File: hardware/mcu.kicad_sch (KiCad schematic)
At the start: 32 parts, among them J3 SW, SW1 BTN_ACT, SW2 BTN_DEACT, U1 STM32F103C8T6, Y1 32KHz, Y2 8MHz

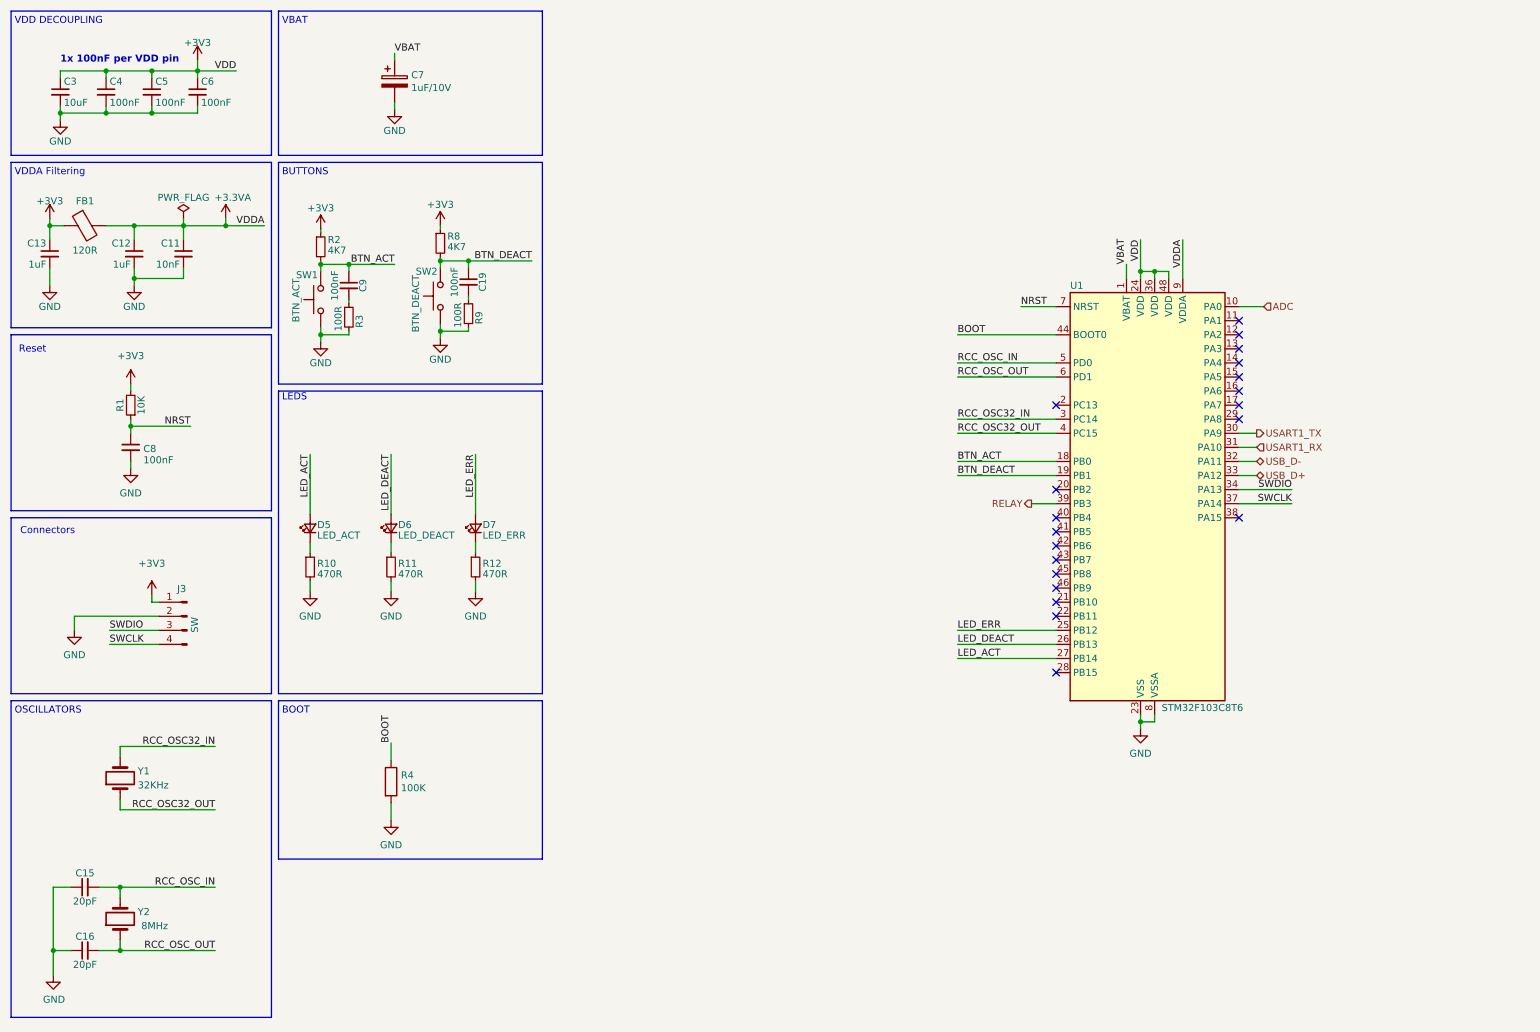
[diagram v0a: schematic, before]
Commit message: * Added an EXP port (contains SPI/I2C/UART/2PINS GPIO/3V3/5V) to the MCU module * USB port connections completed * The Modules are connected to MCU module
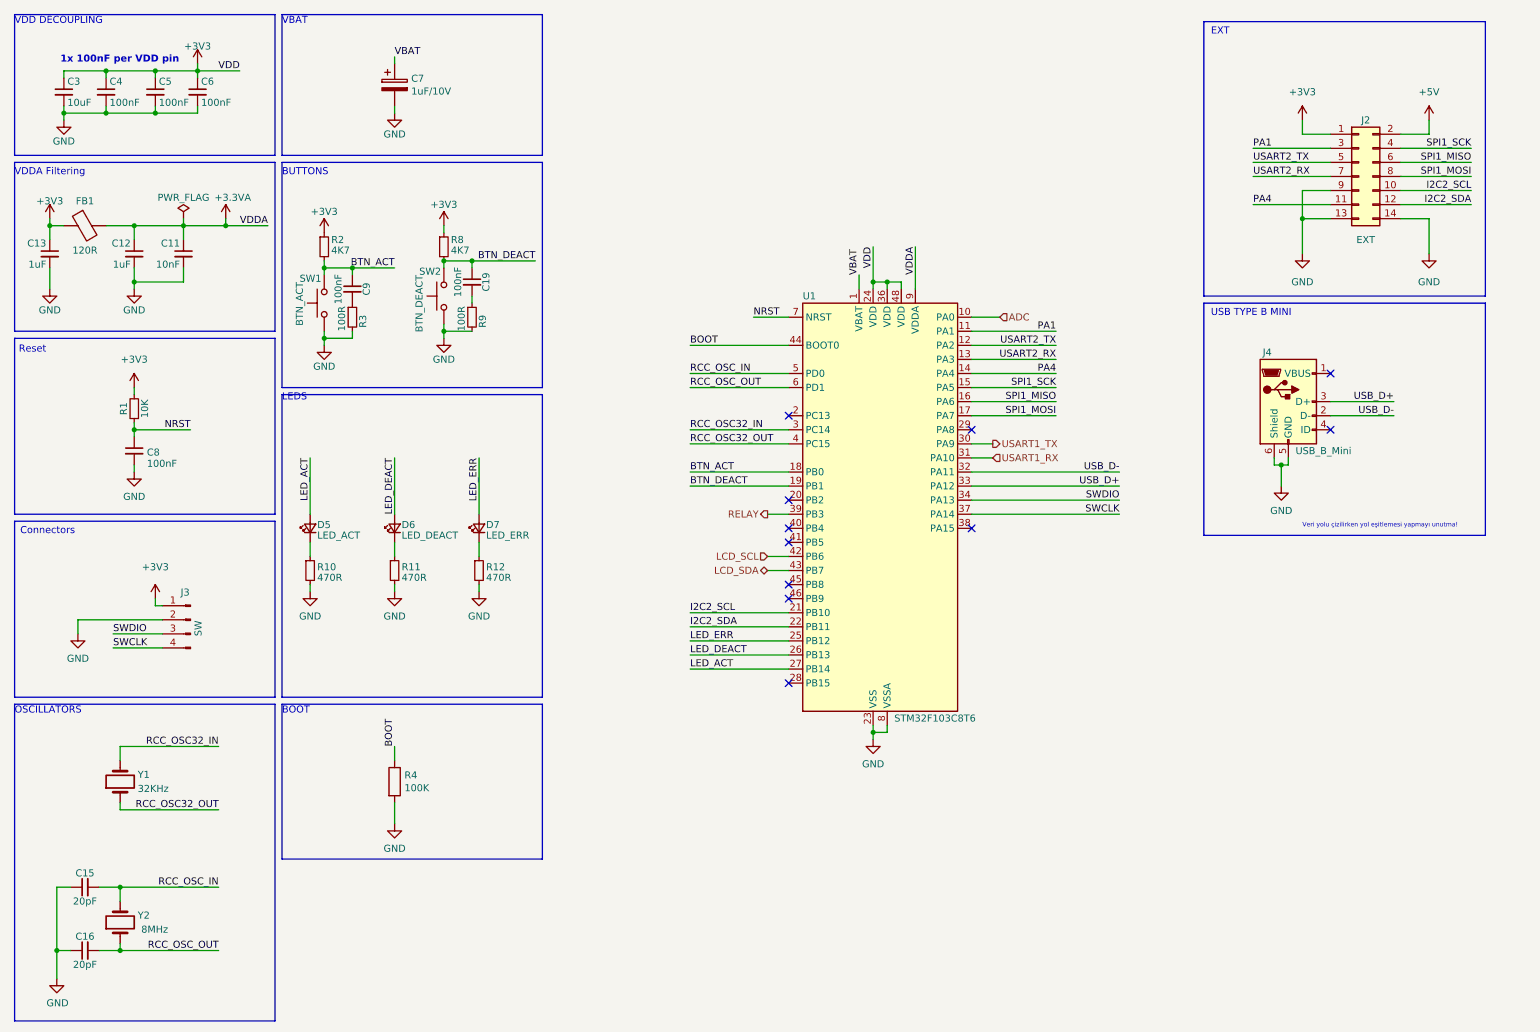
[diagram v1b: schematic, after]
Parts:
- added J2: EXT, symbol Connector_Generic:Conn_02x07_Odd_Even
- added J4: USB_B_Mini, symbol Connector:USB_B_Mini
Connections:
- net +3V3: now also J2.1 (Pin_1)
- net GND: now also J2.13 (Pin_13), J2.14 (Pin_14), J2.9 (Pin_9), J4.5 (GND), J4.6 (Shield)
- net USB_D+: now also J4.3 (D+)
- net USB_D-: now also J4.2 (D-)
- net PA1: now reaches U1.11 (PA1)
- net PA1: now also J2.3 (Pin_3)
- net USART2_TX: now reaches U1.12 (PA2)
- net USART2_TX: now also J2.5 (Pin_5)
- net USART2_RX: now reaches U1.13 (PA3)
- net USART2_RX: now also J2.7 (Pin_7)
- net PA4: now reaches U1.14 (PA4)
- net PA4: now also J2.11 (Pin_11)
- net SPI1_SCK: now reaches U1.15 (PA5)
- net SPI1_SCK: now also J2.4 (Pin_4)
- net SPI1_MISO: now reaches U1.16 (PA6)
- net SPI1_MISO: now also J2.6 (Pin_6)
- net SPI1_MOSI: now reaches U1.17 (PA7)
- net SPI1_MOSI: now also J2.8 (Pin_8)
- net I2C2_SCL: now reaches U1.21 (PB10)
- net I2C2_SCL: now also J2.10 (Pin_10)
- net I2C2_SDA: now reaches U1.22 (PB11)
- net I2C2_SDA: now also J2.12 (Pin_12)
- net LCD_SCL: now reaches U1.42 (PB6)
- net LCD_SDA: now reaches U1.43 (PB7)
- new net +5V: J2.2 (Pin_2)
- no-connect marks 20 -> 11
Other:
- note added: "EXT"
- note added: "USB TYPE B MINI"
- note added: "Veri yolu çizilirken yol eşitlemesi yapmayı unutma!"
- moved on the sheet: C19, C3, C5, C7, C8, C9, D6, D7, J3, R1, R10, R11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
